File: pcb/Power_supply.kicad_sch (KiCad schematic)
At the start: 33 parts, among them Q1 Si4368DY, SW1 POWER, U1 LTC3872, U2 uA78M33

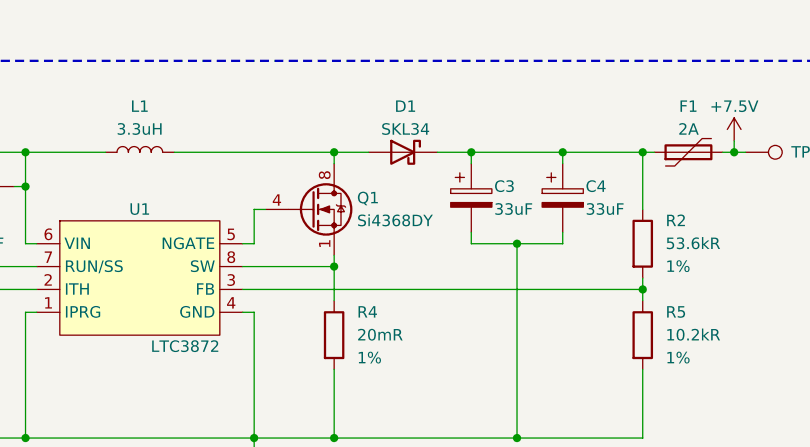
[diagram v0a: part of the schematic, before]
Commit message: [pcb] Change Schottky diode
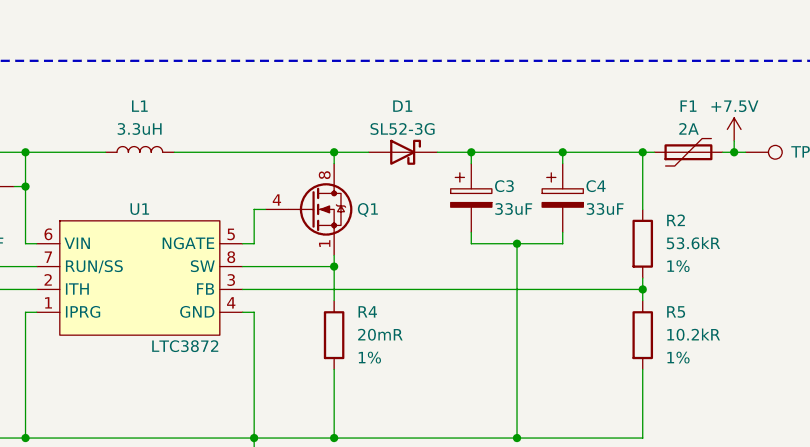
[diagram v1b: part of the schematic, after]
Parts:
- D1: value SKL34 -> SL52-3G; footprint Diode_SMD:D_SOD-123F -> Diode_SMD:D_SMB
- Q1: value Si4368DY -> ~
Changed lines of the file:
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@@
   )
   (symbol (lib_id "Device:D_Schottky") (at 154.94 29.21 0) (mirror y) (unit 1)
-    (in_bom yes) (on_board yes) (dnp no) (fields_autoplaced)
-    (property "Reference" "D1" (at 155.2575 24.13 0)
-      (effects (font (size 1.27 1.27)))
-    )
-    (property "Value" "SKL34" (at 155.2575 26.67 0)
-      (effects (font (size 1.27 1.27)))
-    )
-    (property "Footprint" "Diode_SMD:D_SOD-123F" (at 154.94 29.21 0)
+    (in_bom yes) (on_board yes) (dnp no)
+    (property "Reference" "D1" (at 154.94 24.13 0)
+      (effects (font (size 1.27 1.27)))
+    )
+    (property "Value" "SL52-3G" (at 154.94 26.67 0)
+      (effects (font (size 1.27 1.27)))
+    )
+    (property "Footprint" "Diode_SMD:D_SMB" (at 154.94 29.21 0)
       (effects (font (size 1.27 1.27)) hide)
     )
@@
   (symbol (lib_id "Autko:Si4368DY") (at 144.78 35.56 0) (unit 1)
     (in_bom yes) (on_board yes) (dnp no)
-    (property "Reference" "Q1" (at 149.86 34.29 0)
-      (effects (font (size 1.27 1.27)) (justify left))
-    )
-    (property "Value" "Si4368DY" (at 149.86 36.83 0)
-      (effects (font (size 1.27 1.27)) (justify left))
+    (property "Reference" "Q1" (at 149.86 35.56 0)
+      (effects (font (size 1.27 1.27)) (justify left))
+    )
+    (property "Value" "~" (at 149.86 36.83 0)
+      (effects (font (size 1.27 1.27)) (justify left) hide)
     )
     (property "Footprint" "Package_SO:SO-8_3.9x4.9mm_P1.27mm" (at 149.86 39.37 0)

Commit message: [pcb] Inductor upgrade, boost converter clean-up
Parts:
- L1: footprint Inductor_SMD:L_10.4x10.4_H4.8 -> Inductor_SMD:L_12x12mm_H6mm
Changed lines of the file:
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@@
       (effects (font (size 1.27 1.27)))
     )
-    (property "Footprint" "Inductor_SMD:L_10.4x10.4_H4.8" (at 125.73 29.21 0)
+    (property "Footprint" "Inductor_SMD:L_12x12mm_H6mm" (at 125.73 29.21 0)
       (effects (font (size 1.27 1.27)) hide)
     )

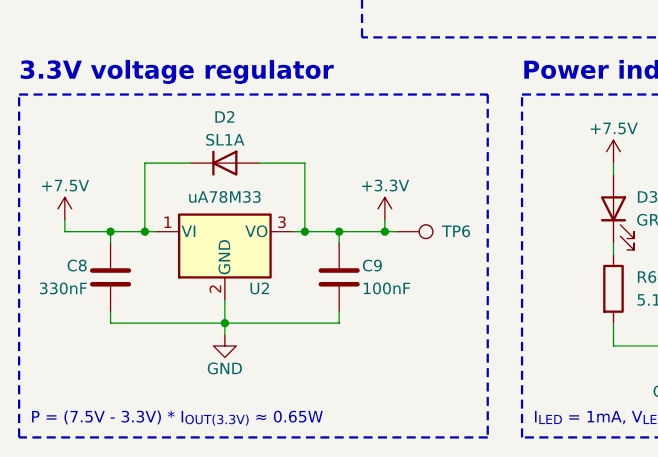
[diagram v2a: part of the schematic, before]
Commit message: [pcb] Voltage regulator changed to TLV761
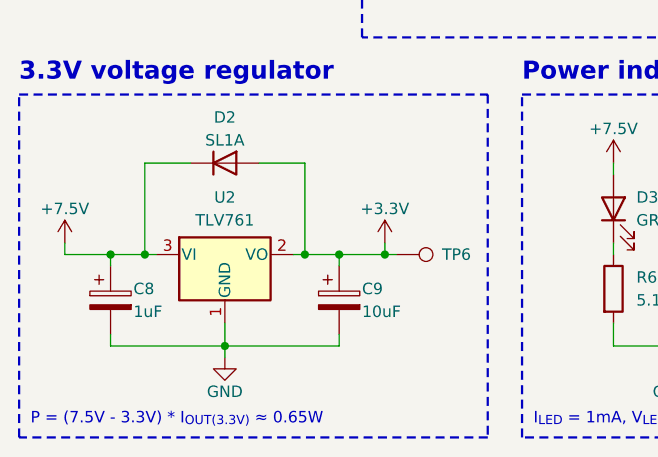
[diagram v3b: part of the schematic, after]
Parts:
- removed C8: 330nF, Capacitor_SMD:C_0805_2012Metric, symbol Device:C
- removed C9: 100nF, Capacitor_SMD:C_0805_2012Metric, symbol Device:C
- removed U2: uA78M33, Package_TO_SOT_SMD:SOT-223-3_TabPin2, symbol Autko:uA78M33
- added C8: 1uF, Capacitor_Tantalum_SMD:CP_EIA-3528-21_Kemet-B, symbol Device:C_Polarized
- added C9: 10uF, Capacitor_Tantalum_SMD:CP_EIA-3216-18_Kemet-A, symbol Device:C_Polarized
- added U2: TLV761, Package_TO_SOT_SMD:SOT-223-3_TabPin2, symbol Autko:TLV761
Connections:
- net +3.3V: now also C9.1, U2.2 (VO)
- net +7.5V: now also C8.1, U2.3 (VI)
- net GND: now also C8.2, C9.2, U2.1 (GND)
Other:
- moved on the sheet: TP6

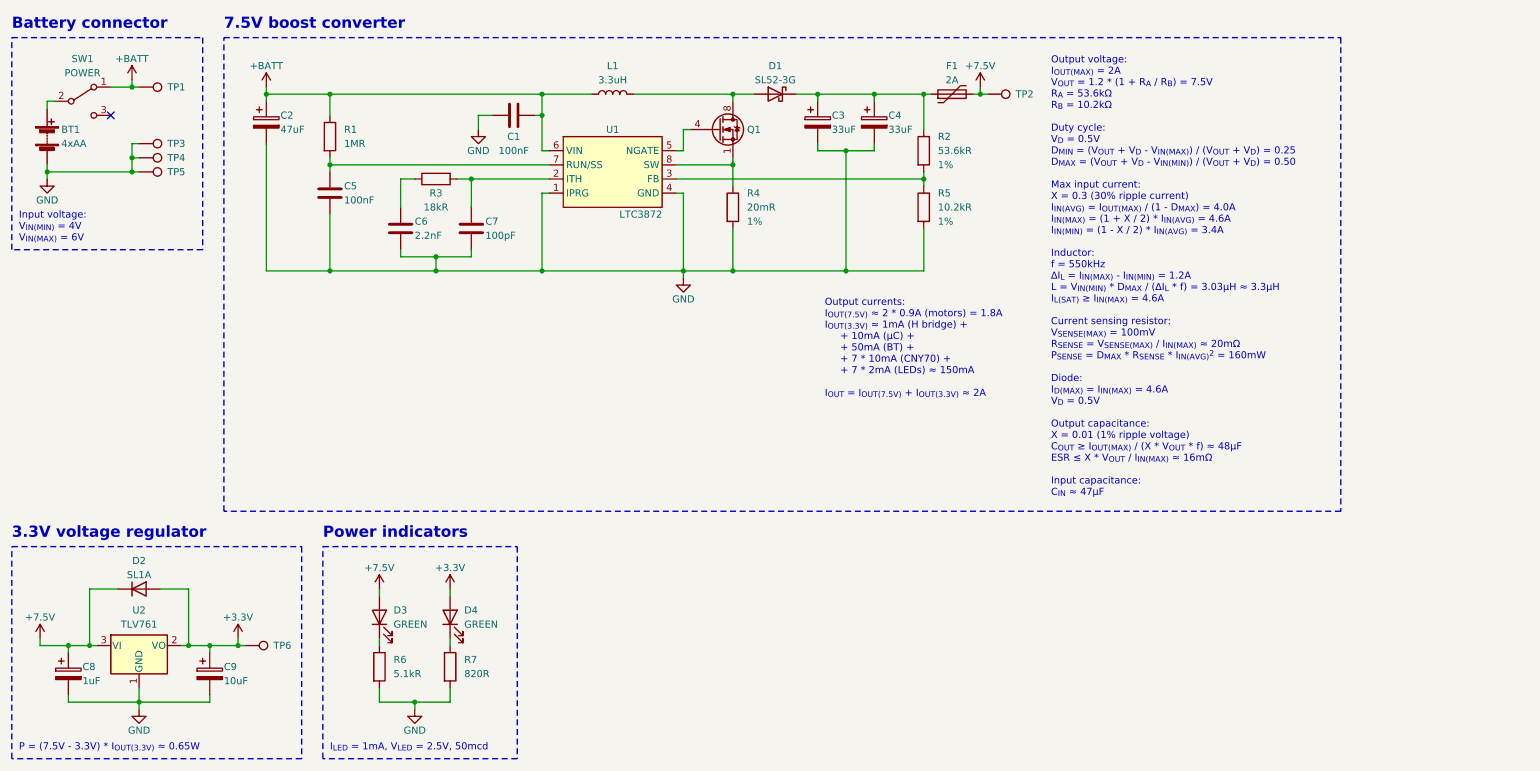
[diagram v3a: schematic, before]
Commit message: [pcb] Test points reduced to 1.5mm; flow control series resistors added
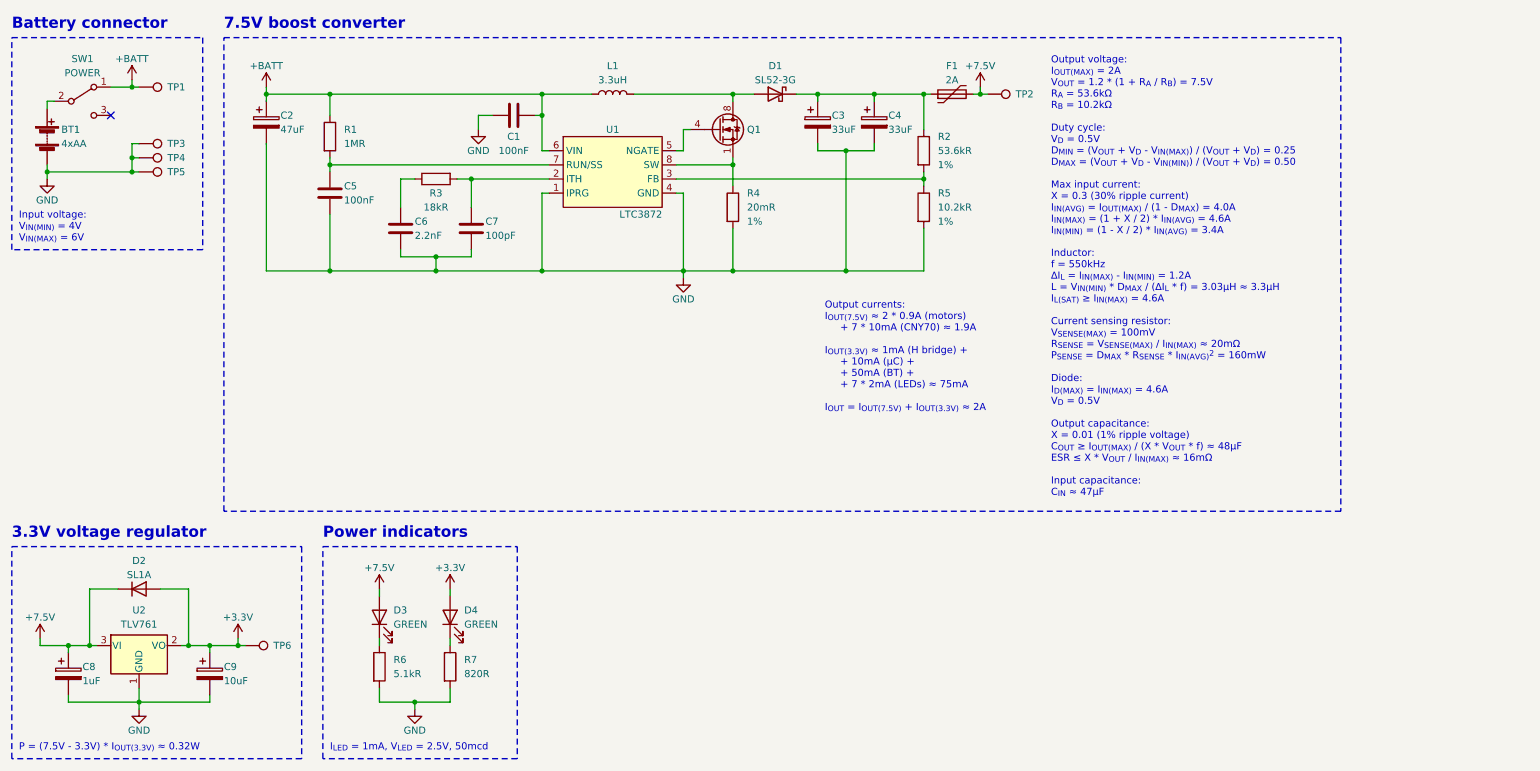
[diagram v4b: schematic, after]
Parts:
- TP1, TP2, TP6: footprint TestPoint:TestPoint_Pad_D2.0mm -> TestPoint:TestPoint_Pad_D1.5mm
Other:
- note added: "Output currents: I_{OUT(7.5V)} ≈ 2 * 0.9A (motors) + 7 * 10mA (CNY70) ≈ 1.9A I_{OUT(3.3V)} ≈ 1mA (H bridge) + + 10mA (µC) + + 50mA (BT) + + 7 * 2mA (LEDs) ≈ 75mA I_{OUT} = I_{OUT(7.5V)} + I_{OUT(3.3V)} ≈ 2A"
- note added: "P = (7.5V - 3.3V) * I_{OUT(3.3V)} ≈ 0.32W"
- note removed: "Output currents: I_{OUT(7.5V)} ≈ 2 * 0.9A (motors) = 1.8A I_{OUT(3.3V)} ≈ 1mA (H bridge) + + 10mA (µC) + + 50mA (BT) + + 7 * 10mA (CNY70) + + 7 * 2mA (LEDs) ≈ 150mA I_{OUT} = I_{OUT(7.5V)} + I_{OUT(3.3V)} ≈ 2A"
- note removed: "P = (7.5V - 3.3V) * I_{OUT(3.3V)} ≈ 0.65W"
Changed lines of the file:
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@@
     (fill (type none))
   )
-  (text "P = (7.5V - 3.3V) * I_{OUT(3.3V)} ≈ 0.65W\n" (at 19.05 147.32 0)
+  (text "P = (7.5V - 3.3V) * I_{OUT(3.3V)} ≈ 0.32W\n" (at 19.05 147.32 0)
     (effects (font (size 1.27 1.27)) (justify left bottom))
   )
@@
     (effects (font (size 2 2) (thickness 0.4) bold) (justify left bottom))
   )
-  (text "Output currents:\nI_{OUT(7.5V)} ≈ 2 * 0.9A (motors) = 1.8A\nI_{OUT(3.3V)} ≈ 1mA (H bridge) +\n     + 10mA (µC) +\n     + 50mA (BT) +\n     + 7 * 10mA (CNY70) +\n     + 7 * 2mA (LEDs) ≈ 150mA\n\nI_{OUT} = I_{OUT(7.5V)} + I_{OUT(3.3V)} ≈ 2A"
-    (at 163.83 83.82 0)
+  (text "Output currents:\nI_{OUT(7.5V)} ≈ 2 * 0.9A (motors)\n     + 7 * 10mA (CNY70) ≈ 1.9A\n\nI_{OUT(3.3V)} ≈ 1mA (H bridge) +\n     + 10mA (µC) +\n     + 50mA (BT) +\n     + 7 * 2mA (LEDs) ≈ 75mA\n\nI_{OUT} = I_{OUT(7.5V)} + I_{OUT(3.3V)} ≈ 2A"
+    (at 163.83 86.36 0)
     (effects (font (size 1.27 1.27)) (justify left bottom))
   )
@@
       (effects (font (size 1.27 1.27)) (justify left) hide)
     )
-    (property "Footprint" "TestPoint:TestPoint_Pad_D2.0mm" (at 193.04 34.29 0)
+    (property "Footprint" "TestPoint:TestPoint_Pad_D1.5mm" (at 193.04 34.29 0)
       (effects (font (size 1.27 1.27)) hide)
     )
@@
       (effects (font (size 1.27 1.27)) (justify left) hide)
     )
-    (property "Footprint" "TestPoint:TestPoint_Pad_D2.0mm" (at 59.69 133.35 0)
+    (property "Footprint" "TestPoint:TestPoint_Pad_D1.5mm" (at 59.69 133.35 0)
       (effects (font (size 1.27 1.27)) hide)
     )
@@
       (effects (font (size 1.27 1.27)) (justify left) hide)
     )
-    (property "Footprint" "TestPoint:TestPoint_Pad_D2.0mm" (at 40.64 33.02 0)
-      (effects (font (size 1.27 1.27)) hide)
-    )
+    (property "Footprint" "TestPoint:TestPoint_Pad_D1.5mm" (at 40.64 33.02 0)
+      (effects (font (size 1.27 1.27)) hide)
+    )

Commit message: [pcb] Assign smaller footprints
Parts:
- C1, C5, C6, C7: footprint Capacitor_SMD:C_0805_2012Metric -> Capacitor_SMD:C_0603_1608Metric
- C8: footprint Capacitor_Tantalum_SMD:CP_EIA-3528-21_Kemet-B -> Capacitor_SMD:C_1206_3216Metric
- C9: footprint Capacitor_Tantalum_SMD:CP_EIA-3216-18_Kemet-A -> Capacitor_SMD:C_1206_3216Metric
- D3, D4: footprint LED_SMD:LED_0805_2012Metric -> LED_SMD:LED_0603_1608Metric
- R1, R2, R3, R5, R6, R7: footprint Resistor_SMD:R_0805_2012Metric -> Resistor_SMD:R_0603_1608Metric
- R4: footprint Resistor_SMD:R_0805_2012Metric -> Resistor_SMD:R_1206_3216Metric
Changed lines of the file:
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@@
       (effects (font (size 1.27 1.27)))
     )
-    (property "Footprint" "Resistor_SMD:R_0805_2012Metric" (at 93.98 42.672 90)
+    (property "Footprint" "Resistor_SMD:R_0603_1608Metric" (at 93.98 42.672 90)
       (effects (font (size 1.27 1.27)) hide)
     )
@@
       (effects (font (size 1.27 1.27)) (justify left))
     )
-    (property "Footprint" "Capacitor_SMD:C_0805_2012Metric" (at 75.8952 50.8 0)
+    (property "Footprint" "Capacitor_SMD:C_0603_1608Metric" (at 75.8952 50.8 0)
       (effects (font (size 1.27 1.27)) hide)
     )
@@
       (effects (font (size 1.27 1.27)) (justify left))
     )
-    (property "Footprint" "Resistor_SMD:R_0805_2012Metric" (at 179.832 39.37 90)
+    (property "Footprint" "Resistor_SMD:R_0603_1608Metric" (at 179.832 39.37 90)
       (effects (font (size 1.27 1.27)) hide)
     )
@@
       (effects (font (size 1.27 1.27)) (justify left))
     )
-    (property "Footprint" "Capacitor_SMD:C_0805_2012Metric" (at 101.2952 57.15 0)
+    (property "Footprint" "Capacitor_SMD:C_0603_1608Metric" (at 101.2952 57.15 0)
       (effects (font (size 1.27 1.27)) hide)
     )
@@
       (effects (font (size 1.27 1.27)) (justify left))
     )
-    (property "Footprint" "Resistor_SMD:R_0805_2012Metric" (at 179.832 49.53 90)
+    (property "Footprint" "Resistor_SMD:R_0603_1608Metric" (at 179.832 49.53 90)
       (effects (font (size 1.27 1.27)) hide)
     )
@@
       (effects (font (size 1.27 1.27)) (justify left))
     )
-    (property "Footprint" "Resistor_SMD:R_0805_2012Metric" (at 94.742 132.08 90)
+    (property "Footprint" "Resistor_SMD:R_0603_1608Metric" (at 94.742 132.08 90)
       (effects (font (size 1.27 1.27)) hide)
     )
@@
       (effects (font (size 1.27 1.27)) (justify left))
     )
-    (property "Footprint" "Capacitor_SMD:C_0805_2012Metric" (at 88.5952 57.15 0)
+    (property "Footprint" "Capacitor_SMD:C_0603_1608Metric" (at 88.5952 57.15 0)
       (effects (font (size 1.27 1.27)) hide)
     )
@@
       (effects (font (size 1.27 1.27)) (justify right))
     )
-    (property "Footprint" "LED_SMD:LED_0805_2012Metric" (at 96.52 123.19 0)
+    (property "Footprint" "LED_SMD:LED_0603_1608Metric" (at 96.52 123.19 0)
       (effects (font (size 1.27 1.27)) hide)
     )
@@
       (effects (font (size 1.27 1.27)) (justify left))
     )
-    (property "Footprint" "Resistor_SMD:R_0805_2012Metric" (at 73.152 36.83 90)
+    (property "Footprint" "Resistor_SMD:R_0603_1608Metric" (at 73.152 36.83 90)
       (effects (font (size 1.27 1.27)) hide)
     )
@@
       (effects (font (size 1.27 1.27)) (justify left))
     )
-    (property "Footprint" "Capacitor_Tantalum_SMD:CP_EIA-3528-21_Kemet-B" (at 28.9052 137.16 0)
+    (property "Footprint" "Capacitor_SMD:C_1206_3216Metric" (at 28.9052 137.16 0)
       (effects (font (size 1.27 1.27)) hide)
     )
@@
       (effects (font (size 1.27 1.27)) (justify right))
     )
-    (property "Footprint" "LED_SMD:LED_0805_2012Metric" (at 83.82 123.19 0)
+    (property "Footprint" "LED_SMD:LED_0603_1608Metric" (at 83.82 123.19 0)
       (effects (font (size 1.27 1.27)) hide)
     )
@@
       (effects (font (size 1.27 1.27)))
     )
-    (property "Footprint" "Capacitor_SMD:C_0805_2012Metric" (at 104.14 33.9852 0)
+    (property "Footprint" "Capacitor_SMD:C_0603_1608Metric" (at 104.14 33.9852 0)
       (effects (font (size 1.27 1.27)) hide)
     )
@@
       (effects (font (size 1.27 1.27)) (justify left))
     )
-    (property "Footprint" "Resistor_SMD:R_0805_2012Metric" (at 145.542 49.53 90)
+    (property "Footprint" "Resistor_SMD:R_1206_3216Metric" (at 145.542 49.53 90)
       (effects (font (size 1.27 1.27)) hide)
     )
@@
       (effects (font (size 1.27 1.27)) (justify left))
     )
-    (property "Footprint" "Resistor_SMD:R_0805_2012Metric" (at 82.042 132.08 90)
+    (property "Footprint" "Resistor_SMD:R_0603_1608Metric" (at 82.042 132.08 90)
       (effects (font (size 1.27 1.27)) hide)
     )
@@
       (effects (font (size 1.27 1.27)) (justify left))
     )
-    (property "Footprint" "Capacitor_Tantalum_SMD:CP_EIA-3216-18_Kemet-A" (at 54.3052 137.16 0)
-      (effects (font (size 1.27 1.27)) hide)
-    )
+    (property "Footprint" "Capacitor_SMD:C_1206_3216Metric" (at 54.3052 137.16 0)
+      (effects (font (size 1.27 1.27)) hide)
+    )
